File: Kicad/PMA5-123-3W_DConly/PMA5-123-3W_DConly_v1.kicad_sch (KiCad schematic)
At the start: 42 parts, among them J1 8V-DC, J2 UPDI, J3 RF_unit, Q1 FMG1, Q2 BC850, SW1 SW_Push, U1 L78L05_SOT89, U2 R05C1TF05S-R, U3 MIC29302, U5 INA168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

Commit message: Update Kicad and SW
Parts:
- removed C12, C2, C5: 10u, Capacitor_SMD:C_0805_2012Metric, symbol Device:C_Polarized
- removed Q2: BC850, Package_TO_SOT_SMD:SOT-23, symbol Device:Q_PNP_BEC
- removed R14: 10K, Resistor_SMD:R_0603_1608Metric, symbol Device:R
- added C12, C2, C5: 10u, Capacitor_SMD:C_0603_1608Metric, symbol Device:C
- added Q2: BC859C, Package_TO_SOT_SMD:SOT-23, symbol Transistor_BJT:BC850
- added R8: 10K, Resistor_SMD:R_0603_1608Metric, symbol Device:R
- C1: value 100n -> 10u; footprint Capacitor_SMD:C_0603_1608Metric -> Capacitor_SMD:C_0805_2012Metric
- C23: value 100n -> 1n
- D1: Mouser (none) -> 750-SS34BF
- F1: Mouser (none) -> 576-1812L200/12DR
- Q1: Mouser (none) -> 755-FMG1AT148
- R1: value 0.05R -> 0.1R; Mouser (none) -> 603-PT2512FK-070R1L
- R3: value 22K -> 2K2
- R4: value 4K7 -> 470R
- R6: value 27K -> 5K1
- R7: value 10K -> 2K
- R9: value 10K -> 100K
- U1: Mouser (none) -> 511-L78L05ABU
- U2: Mouser (none) -> 919-R05C1TF05S-R
- U3: Mouser (none) -> 998-MIC29302WU
- U5: Mouser (none) -> 595-INA168NA/3K
- U6: Mouser (none) -> 579-ATTINY412-SSF
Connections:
- net +5V: now also C2.1
- net GNDREF: now also R2.2, C12.2, C2.2, C5.2; no longer Q1.4 (E1), U2.7 (Sel)
- net at C9.2, R6.1, R7.1: now also Q2.1 (B)
- net at R12.1, R7.2, U2.10 (Vout-)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: now also U2.7 (Sel), C5.1, Q2.3 (C)
- net at R9.1, U5.1, U6.3 (PA7): now also C23.1
- net at U6.5 (PA2): now also R2.1, U3.1 (EN); no longer Q1.3 (B1)
- net at R10.2, U6.6 (~{RESET}/PA0): no longer C23.1
- net at C22.1, J1.1 (Pin_1), Q1.5 (B1): now also R8.1
- net at J3.3 (Pin_3): now also Q2.2 (E)
- net at C1.1, C3.1, D1.1 (K)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: now also R8.2; no longer R2.1
- net at R1.1, R11.1, R3.1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: now also C12.1
- now unconnected: Q1.2 (C1)
- no-connect marks 0 -> 3
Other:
- note added: "1A => 2V"
- note removed: "10A = 1V"
- moved on the sheet: R2

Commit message: Changed symbol Q2
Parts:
- removed Q2: BC859C, Package_TO_SOT_SMD:SOT-23, symbol Transistor_BJT:BC850
- added Q2: BC859C, Package_TO_SOT_SMD:SOT-23, symbol Transistor_BJT:BC859
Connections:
- net at C9.2, R6.1, R7.1: now also Q2.1 (B)
- net at C5.1, R12.1, R7.2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: now also Q2.3 (C)
- net at J3.3 (Pin_3): now also Q2.2 (E)
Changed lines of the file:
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@@
   (junction (at 21.59 135.89) (diameter 0) (color 0 0 0 0)
   )
+  (junction (at 129.54 124.46) (diameter 0) (color 0 0 0 0)
+  )
   (junction (at 149.86 158.75) (diameter 0) (color 0 0 0 0)
-  )
-  (junction (at 129.54 124.46) (diameter 0) (color 0 0 0 0)
   )
   (junction (at 82.55 173.99) (diameter 0) (color 0 0 0 0)
@@
     (pin "9")
   )
-  (symbol (lib_id "Transistor_BJT:BC850") (at 144.78 158.75 180) (unit 1)
-    (in_bom yes) (on_board yes)
-    (property "Reference" "Q2" (id 0) (at 139.7 157.48 0)
-      (effects (font (size 1.27 1.27)) (justify left))
-    )
-    (property "Value" "BC859C" (id 1) (at 139.7 160.02 0)
-      (effects (font (size 1.27 1.27)) (justify left))
-    )
-    (property "Footprint" "Package_TO_SOT_SMD:SOT-23" (id 2) (at 139.7 156.845 0)
-      (effects (font (size 1.27 1.27) italic) (justify left) hide)
-    )
-    (property "Datasheet" "http://www.infineon.com/dgdl/Infineon-BC847SERIES_BC848SERIES_BC849SERIES_BC850SERIES-DS-v01_01-en.pdf?fileId=db3a304314dca389011541d4630a1657" (id 3) (at 144.78 158.75 0)
-      (effects (font (size 1.27 1.27)) (justify left) hide)
-    )
-    (property "Mouser" "771-BC859CW115" (id 4) (at 144.78 158.75 0)
-      (effects (font (size 1.27 1.27)) hide)
-    )
-    (pin "1")
-    (pin "2")
-    (pin "3")
-  )
   (symbol (lib_id "power:GNDREF") (at 82.55 153.67 0) (unit 1)
     (in_bom yes) (on_board yes) (fields_autoplaced)
@@
     (pin "2")
   )
+  (symbol (lib_id "Transistor_BJT:BC859") (at 144.78 158.75 180) (unit 1)
+    (in_bom yes) (on_board yes) (fields_autoplaced)
+    (property "Reference" "Q2" (id 0) (at 139.7 157.4799 0)
+      (effects (font (size 1.27 1.27)) (justify left))
+    )
+    (property "Value" "BC859C" (id 1) (at 139.7 160.0199 0)
+      (effects (font (size 1.27 1.27)) (justify left))
+    )
+    (property "Footprint" "Package_TO_SOT_SMD:SOT-23" (id 2) (at 139.7 156.845 0)
+      (effects (font (size 1.27 1.27) italic) (justify left) hide)
+    )
+    (property "Datasheet" "http://www.infineon.com/dgdl/Infineon-BC857SERIES_BC858SERIES_BC859SERIES_BC860SERIES-DS-v01_01-en.pdf?fileId=db3a304314dca389011541da0e3a1661" (id 3) (at 144.78 158.75 0)
+      (effects (font (size 1.27 1.27)) (justify left) hide)
+    )
+    (pin "1")
+    (pin "2")
+    (pin "3")
+  )
   (symbol (lib_id "Device:LED") (at 129.54 135.89 90) (unit 1)
     (in_bom yes) (on_board yes) (fields_autoplaced)
@@
       (reference "Q1") (unit 2) (value "FMG1") (footprint "MyFootprints:SOT-25_HandSoldering")
     )
-    (path "/2bb5522b-6a9b-40de-9b11-da088340d317"
+    (path "/5310c24a-2318-4f45-a355-85cc240c139f"
       (reference "Q2") (unit 1) (value "BC859C") (footprint "Package_TO_SOT_SMD:SOT-23")
     )

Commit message: Changed value
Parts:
- R9: value 100K -> 51K
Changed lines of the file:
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@@
       (effects (font (size 1.27 1.27)) (justify left))
     )
-    (property "Value" "100K" (id 1) (at 182.88 146.0499 0)
+    (property "Value" "51K" (id 1) (at 182.88 146.0499 0)
       (effects (font (size 1.27 1.27)) (justify left))
     )
@@
     )
     (path "/d579d2e4-a3f5-44e4-98ef-e49c1190581a"
-      (reference "R9") (unit 1) (value "100K") (footprint "Resistor_SMD:R_0603_1608Metric")
+      (reference "R9") (unit 1) (value "51K") (footprint "Resistor_SMD:R_0603_1608Metric")
     )
     (path "/67c1dbd2-e86a-48bb-a02b-9a81d941dc94"

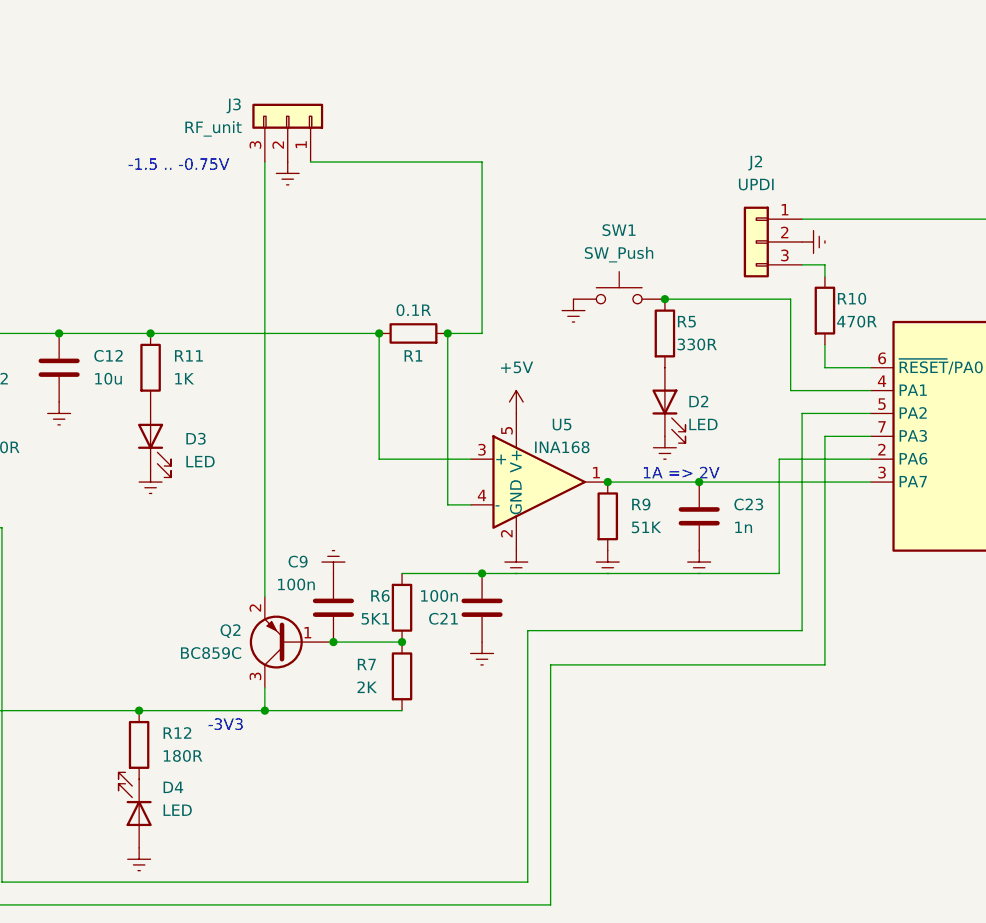
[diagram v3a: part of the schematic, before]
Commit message: Added R13 and JP1
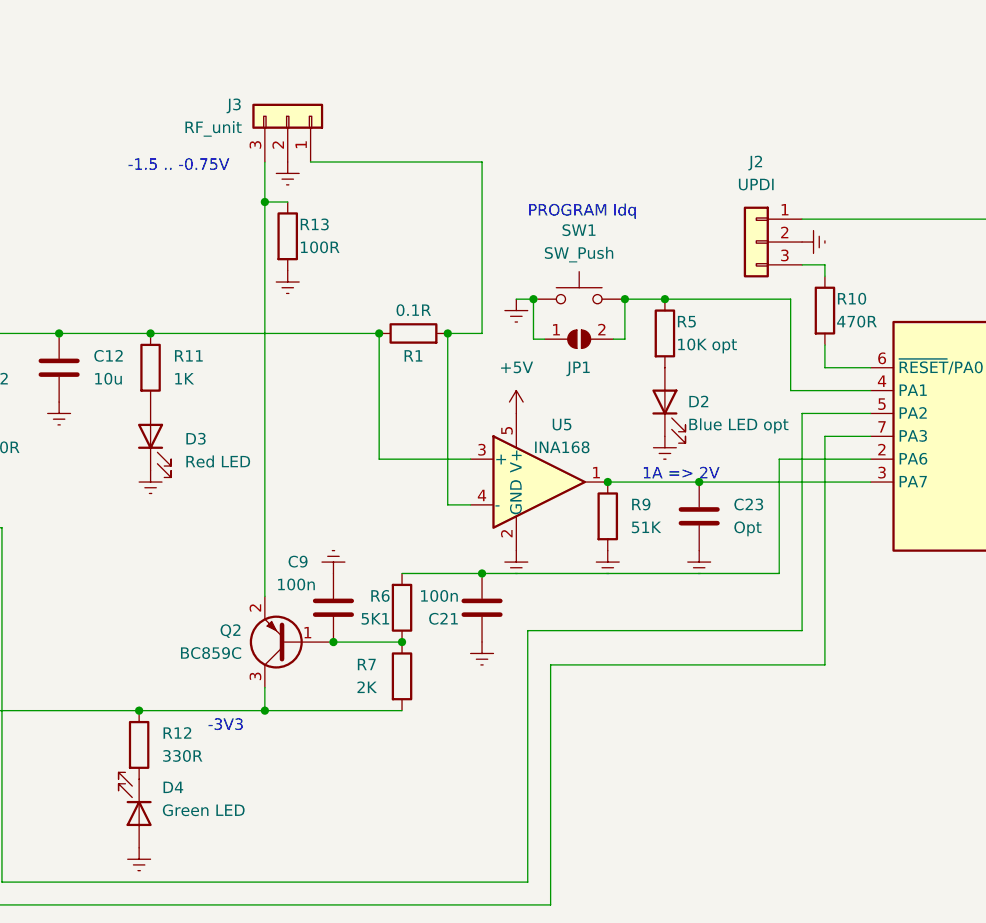
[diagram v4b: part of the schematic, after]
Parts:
- added JP1: ', Jumper:SolderJumper-2_P1.3mm_Open_RoundedPad1.0x1.5mm, symbol Jumper:SolderJumper_2_Open
- added R13: 100R, Resistor_SMD:R_0603_1608Metric, symbol Device:R
- C23: value 1n -> Opt
- D2: value LED -> Blue LED opt
- D3: value LED -> Red LED
- D4: value LED -> Green LED
- R12: value 180R -> 330R
- R5: value 330R -> 10K opt
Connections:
- net GNDREF: now also JP1.1 (A), R13.2
- net at R5.1, SW1.2, U6.4 (PA1): now also JP1.2 (B)
- net at J3.3 (Pin_3), Q2.2 (E): now also R13.1
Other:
- note added: "PROGRAM Idq"
- moved on the sheet: SW1
